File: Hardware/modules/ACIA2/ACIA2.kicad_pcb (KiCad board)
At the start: 4 copper layers, 83.3 x 68.2 mm, 48 parts, among them J1 COM1/3, J2 COM2/4, J3 PORT1, J4 PORT2, J5 Bus_PCI_6502, U1 MAX232, U2 MAX232, U3 6551, U4 MAX232, U5 MAX232, U6 6551, U7 74HC138, U8 74HC138, X1 1.8432MHz

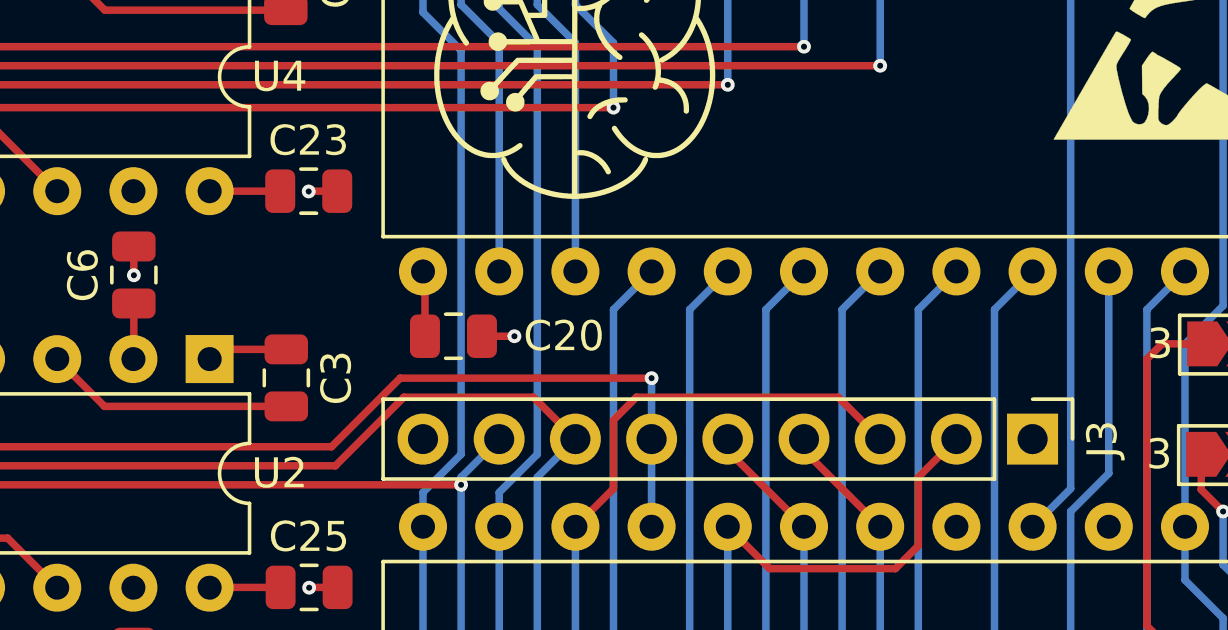
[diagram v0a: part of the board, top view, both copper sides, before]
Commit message: Hardware Update Add MyCPU VGA Module Beautify all Schematics minor Error corrections Readme Update
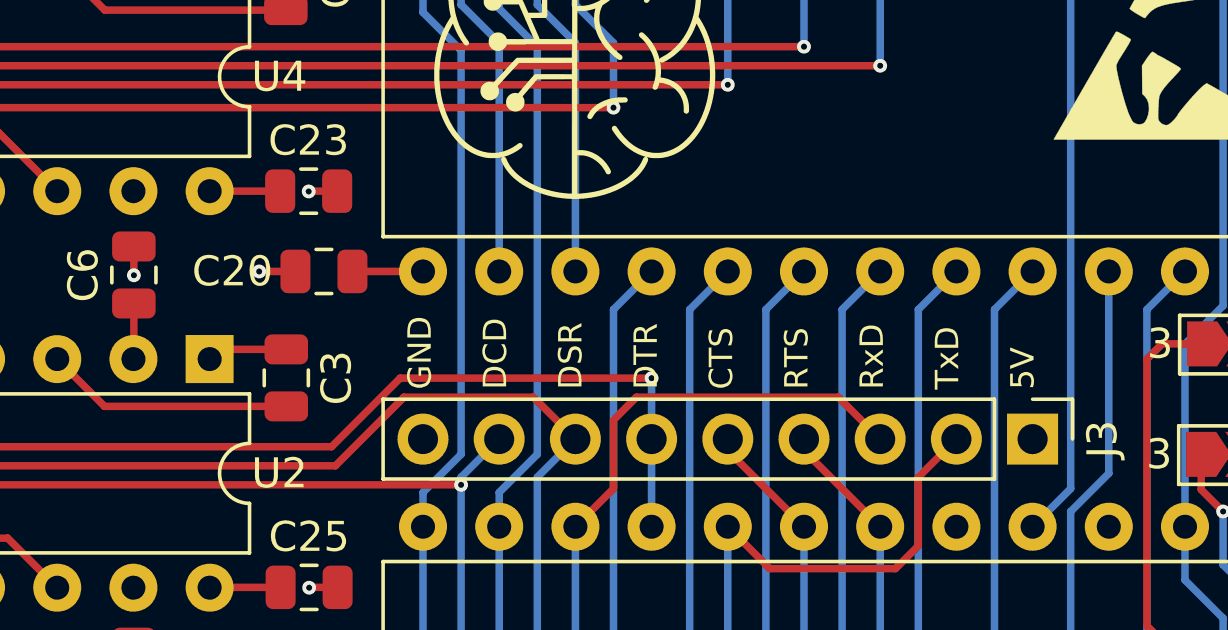
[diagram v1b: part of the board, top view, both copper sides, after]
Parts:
- moved C20 4.83 mm to (130.2, 88.8), turned to 180 degrees
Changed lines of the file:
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@@
 	(footprint "Capacitor_SMD:C_0805_2012Metric"
 		(layer "F.Cu")
-		(at 134.493 90.932)
+		(at 130.175 88.773 180)
 		(descr "Capacitor SMD 0805 (2012 Metric), square (rectangular) end terminal, IPC_7351 nominal, (Body size source: IPC-SM-782 page 76, https://www.pcb-3d.com/wordpress/wp-content/uploads/ipc-sm-782a_amendment_1_and_2.pdf, https://docs.google.com/spreadsheets/d/1BsfQQcO9C6DZCsRaXUlFlo91Tg2WpOkGARC1WS5S8t0/edit?usp=sharing), generated with kicad-footprint-generator")
 		(tags "capacitor")
 		(property "Reference" "C20"
-			(at 3.683 0 0)
+			(at 3.048 0 360)
 			(layer "F.SilkS")
 			(effects
@@
 		)
 		(property "Value" "100n"
-			(at 0 1.68 0)
+			(at 0 1.68 360)
 			(layer "F.Fab")
 			(effects
@@
 		)
 		(property "Footprint" "Capacitor_SMD:C_0805_2012Metric"
-			(at 0 0 0)
+			(at 0 0 180)
 			(unlocked yes)
 			(layer "F.Fab")
@@
 		)
 		(property "Datasheet" ""
-			(at 0 0 0)
+			(at 0 0 180)
 			(unlocked yes)
 			(layer "F.Fab")
@@
 		)
 		(property "Description" "Unpolarized capacitor"
-			(at 0 0 0)
+			(at 0 0 180)
 			(unlocked yes)
 			(layer "F.Fab")
@@
 		(attr smd)
 		(fp_line
-			(start -0.261252 -0.735)
-			(end 0.261252 -0.735)
+			(start -0.261252 0.735)
+			(end 0.261252 0.735)
 			(stroke
 				(width 0.12)
@@
 		)
 		(fp_line
-			(start -0.261252 0.735)
-			(end 0.261252 0.735)
+			(start -0.261252 -0.735)
+			(end 0.261252 -0.735)
 			(stroke
 				(width 0.12)
@@
 		)
 		(fp_line
-			(start -1.7 -0.98)
-			(end 1.7 -0.98)
+			(start 1.7 0.98)
+			(end -1.7 0.98)
 			(stroke
 				(width 0.05)
@@
 		)
 		(fp_line
-			(start -1.7 0.98)
-			(end -1.7 -0.98)
+			(start 1.7 -0.98)
+			(end 1.7 0.98)
 			(stroke
 				(width 0.05)
@@
 		)
 		(fp_line
-			(start 1.7 -0.98)
-			(end 1.7 0.98)
+			(start -1.7 0.98)
+			(end -1.7 -0.98)
 			(stroke
 				(width 0.05)
@@
 		)
 		(fp_line
-			(start 1.7 0.98)
-			(end -1.7 0.98)
+			(start -1.7 -0.98)
+			(end 1.7 -0.98)
 			(stroke
 				(width 0.05)
@@
 		)
 		(fp_line
-			(start -1 -0.625)
-			(end 1 -0.625)
+			(start 1 0.625)
+			(end -1 0.625)
 			(stroke
 				(width 0.1)
@@
 		)
 		(fp_line
-			(start -1 0.625)
-			(end -1 -0.625)
+			(start 1 -0.625)
+			(end 1 0.625)
 			(stroke
 				(width 0.1)
@@
 		)
 		(fp_line
-			(start 1 -0.625)
-			(end 1 0.625)
+			(start -1 0.625)
+			(end -1 -0.625)
 			(stroke
 				(width 0.1)
@@
 		)
 		(fp_line
-			(start 1 0.625)
-			(end -1 0.625)
+			(start -1 -0.625)
+			(end 1 -0.625)
 			(stroke
 				(width 0.1)
@@
 		)
 		(fp_text user "${REFERENCE}"
-			(at 0 0 0)
+			(at 0 0 360)
 			(layer "F.Fab")
 			(effects
@@
 		)
 		(pad "1" smd roundrect
-			(at -0.95 0)
+			(at -0.95 0 180)
 			(size 1 1.45)
 			(layers "F.Cu" "F.Paste" "F.Mask")
@@
 		)
 		(pad "2" smd roundrect
-			(at 0.95 0)
+			(at 0.95 0 180)
 			(size 1 1.45)
 			(layers "F.Cu" "F.Paste" "F.Mask")
@@
 		)
 	)
+	(gr_text "GND\n\nDCD\n\nDSR\n\nDTR\n\nCTS\n\nRTS\n\nRxD\n\nTxD\n\n5V"
+		(at 153.924 92.71 90)
+		(layer "F.SilkS")
+		(effects
+			(font
+				(size 0.78 0.78)
+				(thickness 0.15)
+			)
+			(justify left bottom)
+		)
+	)
 	(gr_text "Port 1"
 		(at 105.537 103.886 90)
@@
 	)
 	(segment
-		(start 135.443 90.932)
-		(end 136.525 90.932)
-		(width 0.25)
-		(layer "F.Cu")
-		(net 2)
-	)
-	(segment
 		(start 129.692 99.304)
 		(end 129.682 99.314)
@@
 	)
 	(segment
+		(start 129.225 88.773)
+		(end 128.016 88.773)
+		(width 0.25)
+		(layer "F.Cu")
+		(net 2)
+	)
+	(segment
 		(start 180.33 97.78)
 		(end 180.34 97.79)
@@
 	)
 	(via
-		(at 136.525 90.932)
-		(size 0.46)
-		(drill 0.2)
-		(layers "F.Cu" "B.Cu")
-		(net 2)
-	)
-	(via
 		(at 154.559 125.095)
 		(size 0.8)
@@
 	)
 	(via
+		(at 128.016 88.773)
+		(size 0.46)
+		(drill 0.2)
+		(layers "F.Cu" "B.Cu")
+		(net 2)
+	)
+	(via
 		(at 126.619 125.095)
 		(size 0.8)
@@
 	)
 	(segment
-		(start 133.543 90.932)
-		(end 133.543 88.839)
+		(start 178.232 94.793)
+		(end 178.181 94.742)
 		(width 0.25)
 		(layer "F.Cu")
@@
 	)
 	(segment
-		(start 178.232 94.793)
-		(end 178.181 94.742)
+		(start 133.477 88.773)
+		(end 131.125 88.773)
 		(width 0.25)
 		(layer "F.Cu")

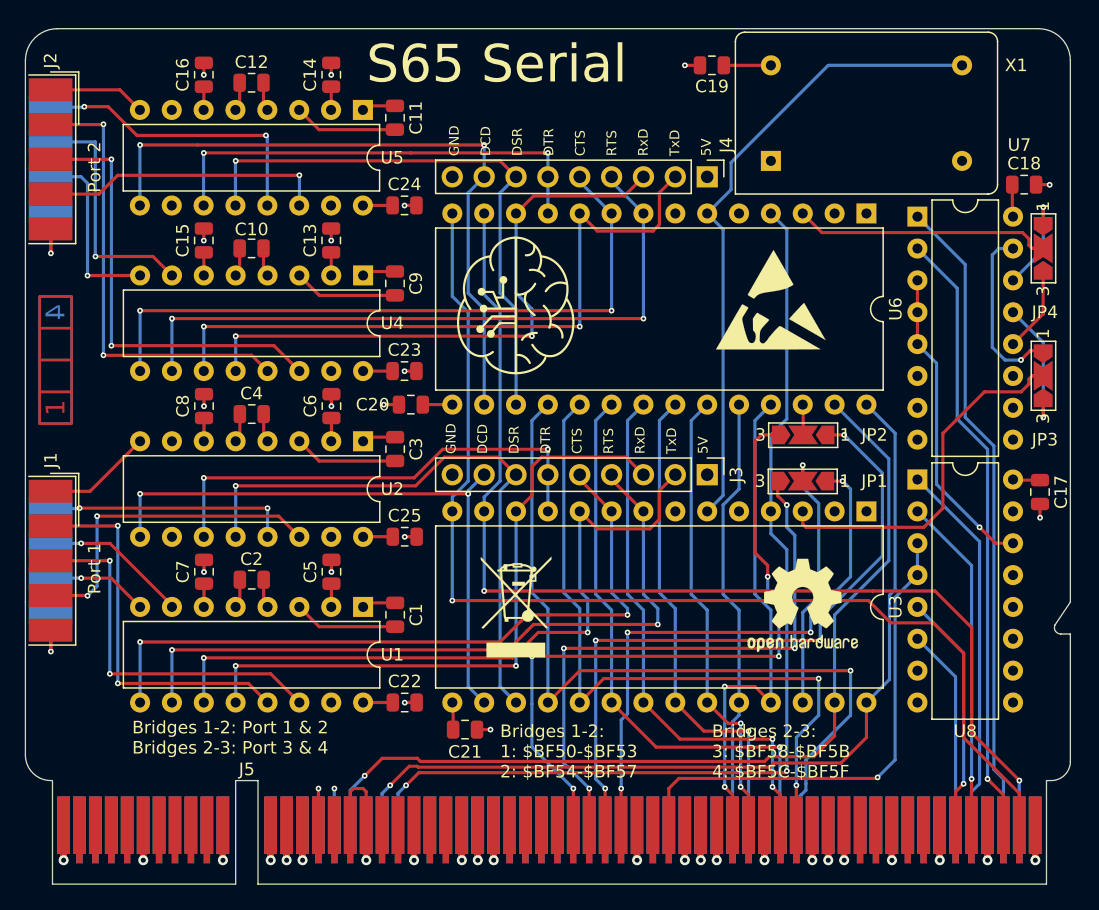
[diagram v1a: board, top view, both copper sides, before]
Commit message: Hardware Review Pt. 1 fix Address Decoding for Strobe Generators add bulk capacitance to every board fix wiring of Prototyping Board
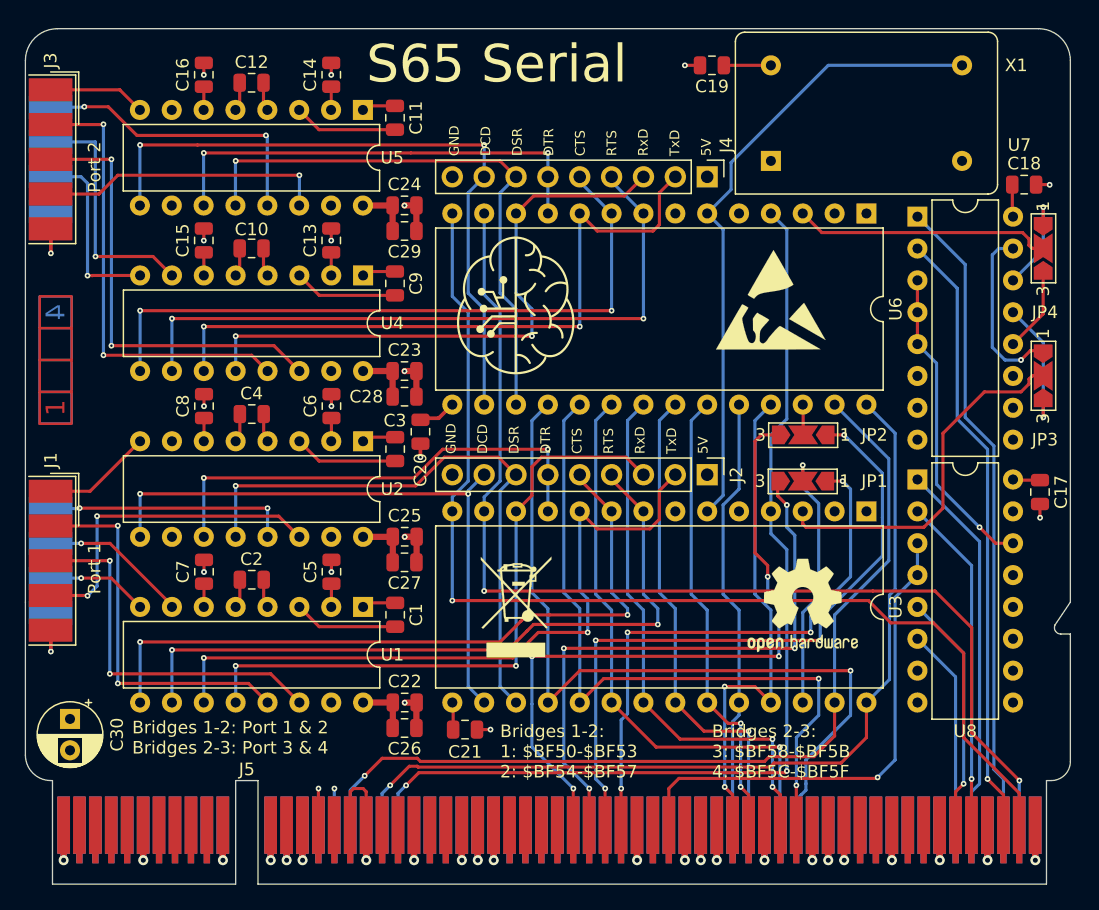
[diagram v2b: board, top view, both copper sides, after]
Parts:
- added C26: 4µ7, Capacitor_SMD:C_0805_2012Metric, F.Cu at (129.7, 114.6)
- added C27: 4µ7, Capacitor_SMD:C_0805_2012Metric, F.Cu at (129.7, 101.3)
- added C28: 4µ7, Capacitor_SMD:C_0805_2012Metric, F.Cu at (129.7, 88.1)
- added C29: 4µ7, Capacitor_SMD:C_0805_2012Metric, F.Cu at (129.7, 74.9)
- added C30: 10µ, Capacitor_THT:CP_Radial_D5.0mm_P2.50mm, F.Cu at (103.0, 113.8)
- JP4: value ACIA1/3 -> ACIA2/4
- moved C20 2.29 mm to (130.9, 90.9), turned to -90 degrees
- renumbered J3 to J2, J2 to J3
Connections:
- J5 pad A11: /A13 -> unconnected-(J5-A13-PadA11)
- J5 pad A12: /A15 -> unconnected-(J5-A15-PadA12)_0
- J5 pad A25: /~{ROM} -> unconnected-(J5-~{ROM}-PadA25)_0
- J5 pad A31: /~{IRQ_0.4} -> unconnected-(J5-~{IRQ_0.4}-PadA31)
- J5 pad A32: /~{IRQ_0.5} -> unconnected-(J5-~{IRQ_0.5}-PadA32)
- J5 pad A33: /~{IRQ_0.6} -> unconnected-(J5-~{IRQ_0.6}-PadA33)_0
- J5 pad A34: /~{IRQ_0.7} -> unconnected-(J5-~{IRQ_0.7}-PadA34)_0
- J5 pad A38: /SYNC_VPA -> unconnected-(J5-Sync/VPA-PadA38)_0
- J5 pad A39: /Ø2/VDA -> unconnected-(J5-Ø2/VDA-PadA39)_0
- J5 pad A41: /~{RDY} -> unconnected-(J5-~{RDY}-PadA41)_0
- J5 pad A42: /~{BE} -> unconnected-(J5-~{BE}-PadA42)
- J5 pad A45: /E -> unconnected-(J5-E-PadA45)_0
- J5 pad A53: /RAM_0 -> unconnected-(J5-RAM0-PadA53)
- J5 pad A54: /RAM_1 -> unconnected-(J5-RAM1-PadA54)
- J5 pad A55: /RAM_2 -> unconnected-(J5-RAM2-PadA55)
- J5 pad A56: /RAM_3 -> unconnected-(J5-RAM3-PadA56)_0
- J5 pad A58: /RAM_4 -> unconnected-(J5-RAM4-PadA58)_0
- J5 pad A59: /RAM_5 -> unconnected-(J5-RAM5-PadA59)_0
- J5 pad A60: /RAM_6 -> unconnected-(J5-RAM6-PadA60)_0
- J5 pad A61: /RAM_7 -> unconnected-(J5-RAM7-PadA61)
- J5 pad A8: /A9 -> unconnected-(J5-A9-PadA8)
- J5 pad A9: /A11 -> unconnected-(J5-A11-PadA9)
- J5 pad B11: /A12 -> unconnected-(J5-A12-PadB11)
- J5 pad B12: /A14 -> unconnected-(J5-A14-PadB12)_0
- J5 pad B24: /~{L_RAM} -> unconnected-(J5-~{L_RAM}-PadB24)_0
- J5 pad B25: /~{H_RAM} -> unconnected-(J5-~{H_RAM}-PadB25)_0
- J5 pad B27: /~{IRQ} -> unconnected-(J5-~{IRQ}-PadB27)
- J5 pad B28: /~{IRQ_0} -> unconnected-(J5-~{IRQ_0}-PadB28)
- J5 pad B29: /~{IRQ_1} -> unconnected-(J5-~{IRQ_1}-PadB29)_0
- J5 pad B30: /~{IRQ_2} -> unconnected-(J5-~{IRQ_2}-PadB30)
- J5 pad B31: /~{IRQ_3} -> unconnected-(J5-~{IRQ_3}-PadB31)_0
- J5 pad B32: /~{IRQ_4} -> unconnected-(J5-~{IRQ_4}-PadB32)_0
- J5 pad B33: /~{NMI} -> unconnected-(J5-~{NMI}-PadB33)
- J5 pad B34: /PAGE -> unconnected-(J5-PAGE_ROM-PadB34)
- J5 pad B38: /~{VP} -> unconnected-(J5-~{VP}-PadB38)
- J5 pad B39: /~{ML} -> unconnected-(J5-~{ML}-PadB39)
- J5 pad B46: /M/X -> unconnected-(J5-M/~{X}-PadB46)_0
- J5 pad B53: /ROM_0 -> unconnected-(J5-ROM0-PadB53)_0
- J5 pad B54: /ROM_1 -> unconnected-(J5-ROM1-PadB54)
- J5 pad B55: /ROM_2 -> unconnected-(J5-ROM2-PadB55)_0
- J5 pad B56: /ROM_3 -> unconnected-(J5-ROM3-PadB56)
- J5 pad B58: /ROM_4 -> unconnected-(J5-ROM4-PadB58)_0
- J5 pad B59: /ROM_5 -> unconnected-(J5-ROM5-PadB59)_0
- J5 pad B60: /ROM_6 -> unconnected-(J5-ROM6-PadB60)_0
- J5 pad B61: /ROM_7 -> unconnected-(J5-ROM7-PadB61)_0
- J5 pad B8: /A8 -> unconnected-(J5-A8-PadB8)
- J5 pad B9: /A10 -> unconnected-(J5-A10-PadB9)
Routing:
- net +5V: track 22.6 -> 31.3 mm
- net GND: track 33.5 -> 41.7 mm

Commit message: Big Review Update - Changed Copper Pours on all PCBs - Implemented errors found at review - fixed some additional errors
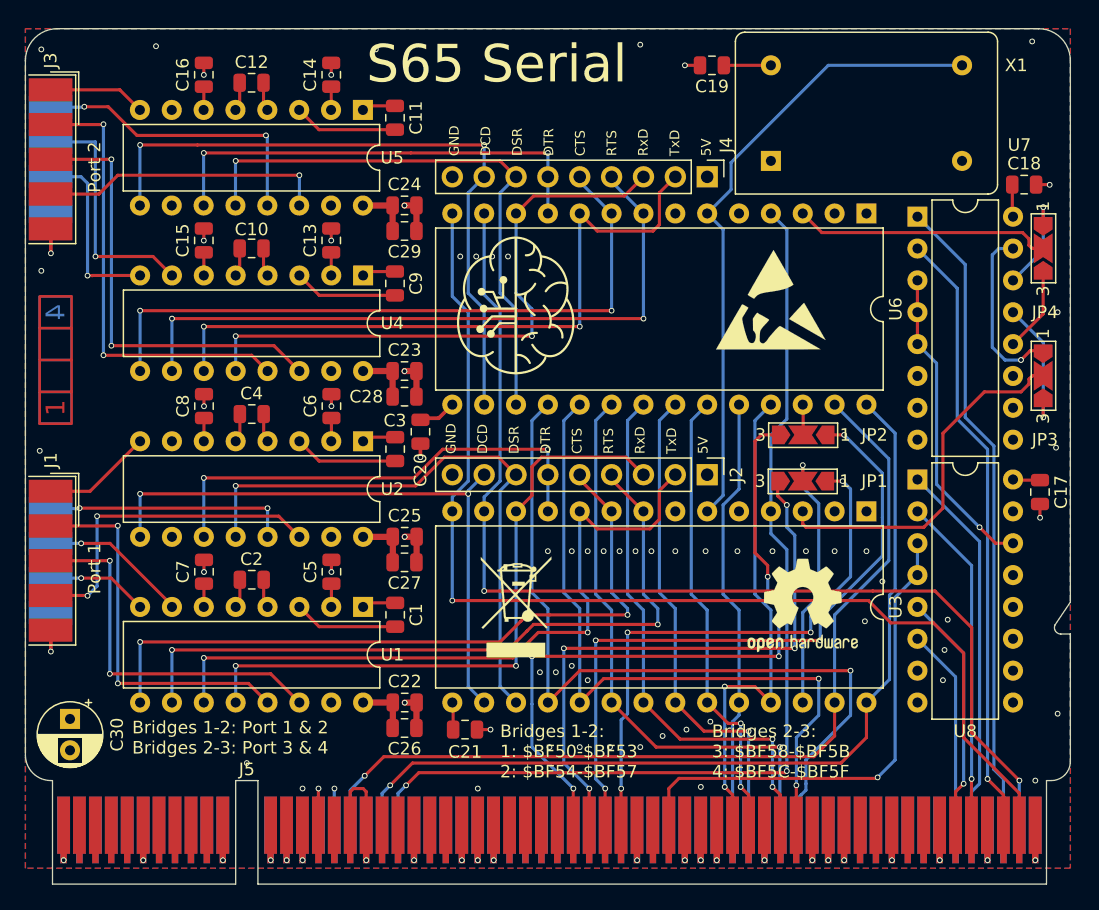
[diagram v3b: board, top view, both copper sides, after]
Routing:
- net +5V: vias 4 -> 53
- added copper zone on B.Cu, net +5V
- added copper zone on F.Cu, net +5V
- added copper zone on In1.Cu, net GND
- removed copper zone on In1.Cu, net +5V
